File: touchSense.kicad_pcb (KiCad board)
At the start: 2 copper layers, 100 x 100 mm, 19 parts, among them J1 breakout_MainBoard, J2 CAPTOUC_castellated_Module, J3 CAPTOUC_castellated_Module, J4 CAPTOUC_castellated_Module, J5 CAPTOUC_castellated_Module, J6 CAPTOUC_castellated_Module, M101 Mount, M102 Mount, M103 Mount

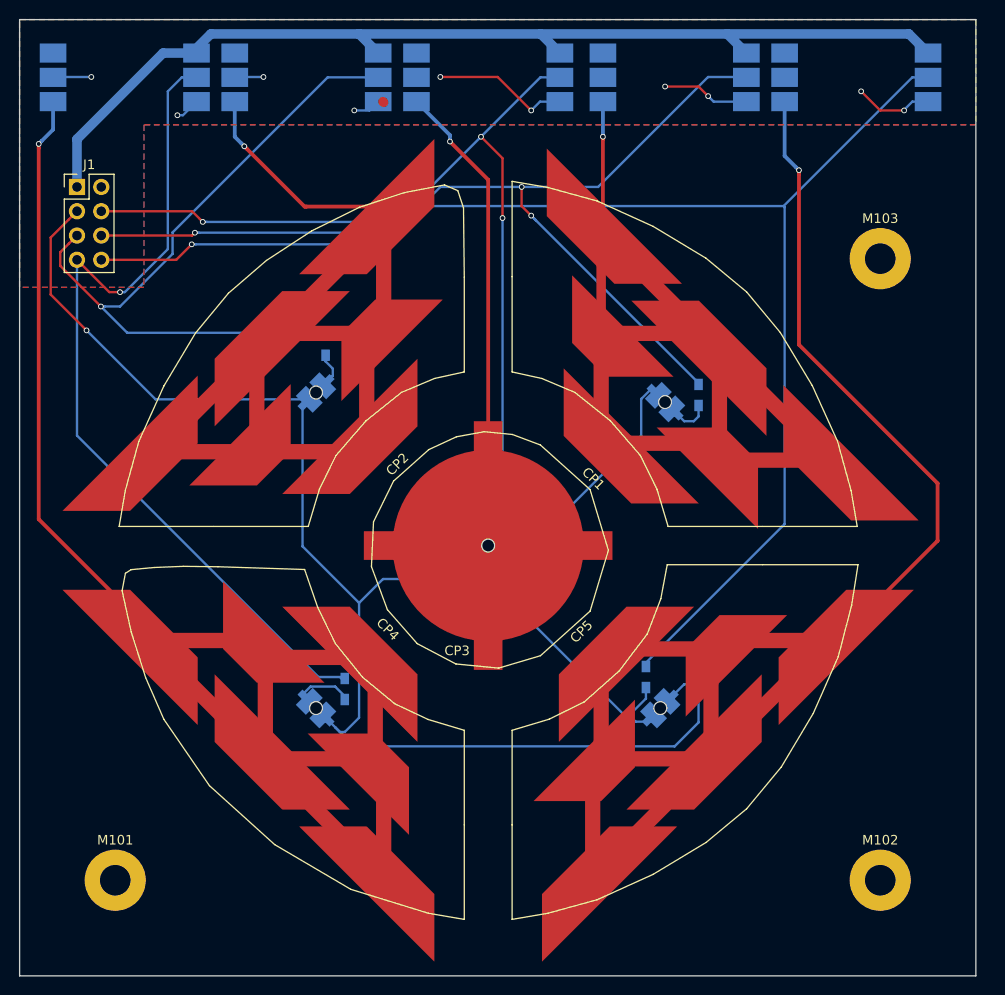
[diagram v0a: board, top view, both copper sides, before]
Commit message: new touch implementation
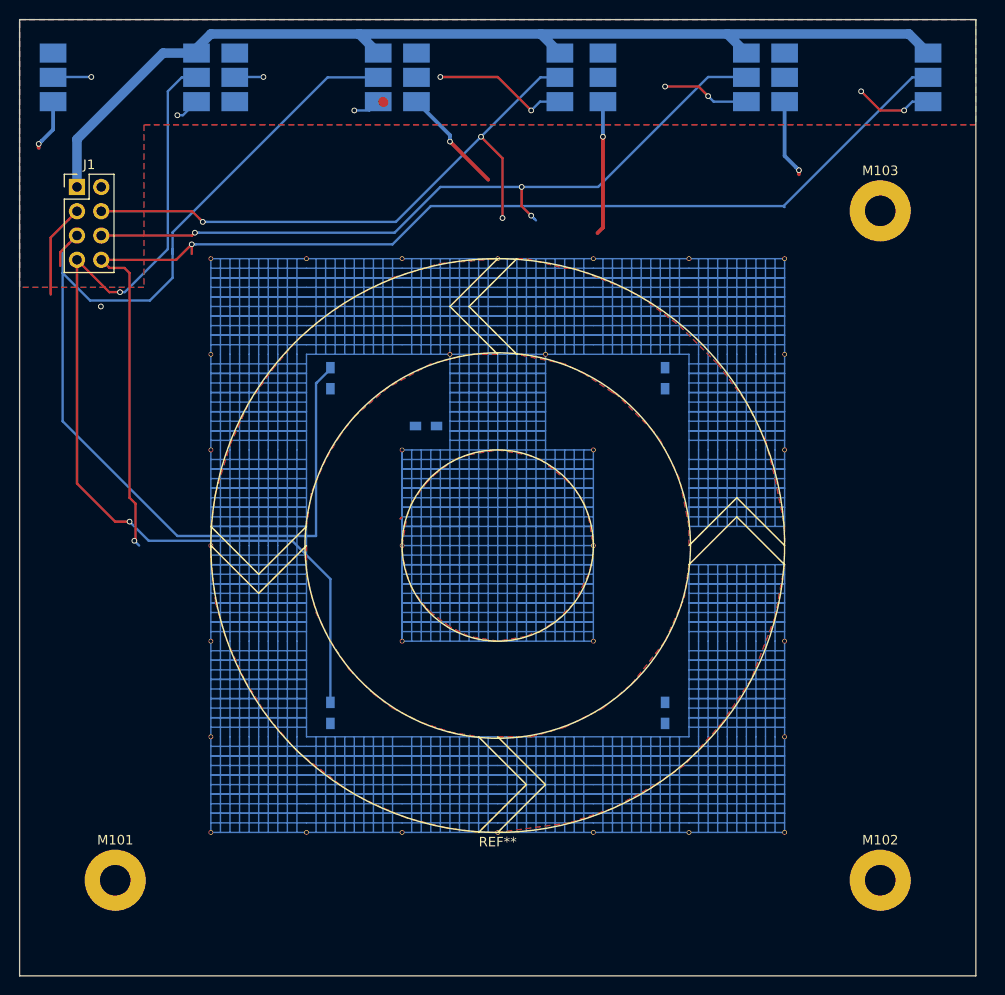
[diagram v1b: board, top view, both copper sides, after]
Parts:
- removed CP1, CP2, CP4, CP5: CAP_PAD_LED, seniorDesign:capacitive_touch_pad_r2
- removed CP3: CAP_PAD_LED, seniorDesign:capacitive_touch_pad_r4
- added J101: HATCHED_FILL, seniorDesign:HATCHED_FILL_60mm_signalRouting, B.Cu at (150.0, 105.0)
- added REF**: CAP_PAD_5POS, seniorDesign:CAP_PAD_5POS_Outline, F.Cu at (150.0, 105.0)
- moved R3 9.42 mm to (142.5, 92.5), turned to 180 degrees
- moved M103 5.00 mm to (190.0, 70.0)
- moved R5 4.25 mm to (167.5, 122.5)
- moved R1 3.91 mm to (167.5, 87.5)
- moved R2 3.54 mm to (132.5, 87.5)
- moved R4 2.92 mm to (132.5, 122.5)
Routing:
- net GND: track 243.5 -> 54.3 mm, vias 11 -> 10
- net /CAP_5: track 174.9 -> 8.22 mm
- net /CAP_4: track 168.4 -> 5.47 mm
- net /CAP_2: track 129.1 -> 0.00 mm, vias 1 -> 0
- net /CAP_1: track 120.1 -> 14.0 mm
- net /CAP_3: track 60.1 -> 11.9 mm
- net /OUT_2: track 75.2 -> 121.0 mm, vias 1 -> 0
- net /OUT_3: track 95.8 -> 64.2 mm
- net /OUT_1: track 103.6 -> 78.8 mm
- net /OUT_5: track 149.8 -> 128.9 mm, vias 1 -> 2
- net /OUT_4: track 89.9 -> 99.8 mm, vias 1 -> 2
- net Net-(CP5-Pad2): track 6.88 -> 0.00 mm
- net Net-(CP4-Pad2): track 6.17 -> 0.00 mm
- net Net-(CP3-Pad2): track 5.85 -> 0.00 mm
- net Net-(CP1-Pad2): track 5.04 -> 0.00 mm
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- added copper zone on F.Cu, net /CAP_1
- added copper zone on F.Cu, net /CAP_2
- added copper zone on F.Cu, net /CAP_4
- added copper zone on F.Cu, net /CAP_5

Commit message: organize project folder, small pcb maitenance, generated gerbers
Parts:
- removed REF**: CAP_PAD_5POS, seniorDesign:CAP_PAD_5POS_Outline
- added D101: LED, seniorDesign:LED_VLRK31Q1R2_REV_GUL, B.Cu at (160.0, 101.0)
- added D102: LED, seniorDesign:LED_VLRK31Q1R2_REV_GUL, B.Cu at (140.0, 101.0)
- added D103: LED, seniorDesign:LED_VLRK31Q1R2_REV_GUL, B.Cu at (150.0, 113.0)
- added D104: LED, seniorDesign:LED_VLRK31Q1R2_REV_GUL, B.Cu at (140.0, 125.0)
- added D105: LED, seniorDesign:LED_VLRK31Q1R2_REV_GUL, B.Cu at (160.0, 125.0)
- added M101: Mount, Mounting_Holes:MountingHole_3.2mm_M3_Pad, F.Cu at (107.0, 83.0)
- J1: moved to B.Cu
- moved J1 45.1 mm to (151.0, 65.0), turned to 180 degrees
- moved R3 20.5 mm to (143.0, 113.0)
- moved R1 19.8 mm to (153.0, 101.0), turned to 180 degrees
- moved R2 18.1 mm to (137.2, 105.0), turned to 270 degrees
- moved M103 13.3 mm to (193.0, 83.0)
- moved J101 8.00 mm to (150.0, 113.0), turned to 0 degrees
- moved R4 4.98 mm to (137.2, 121.0)
- moved R5 4.98 mm to (162.8, 121.0)
- moved M101 4.24 mm to (107.0, 143.0)
- moved M102 4.24 mm to (193.0, 143.0)
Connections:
- J1 pad 4: /OUT_3 -> /OUT_4
- J1 pad 6: /OUT_1 -> /OUT_3
- J1 pad 7: /OUT_4 -> /OUT_1
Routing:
- net GND: track 54.3 -> 166.0 mm, vias 10 -> 2
- net /CAP_2: track 0.00 -> 83.0 mm, vias 0 -> 1
- net /CAP_4: track 5.47 -> 70.0 mm
- net /CAP_5: track 8.22 -> 71.3 mm
- net /OUT_1: track 78.8 -> 140.4 mm, vias 3 -> 1
- net /OUT_5: track 128.9 -> 185.8 mm, vias 2 -> 1
- net /OUT_3: track 64.2 -> 118.1 mm
- net /OUT_4: track 99.8 -> 140.4 mm, vias 2 -> 1
- net /CAP_3: track 11.9 -> 28.9 mm
- net /CAP_1: track 14.0 -> 29.2 mm
- net /OUT_2: track 121.0 -> 132.2 mm, vias 0 -> 2
- net /VCC: track 108.2 -> 98.2 mm
- net Net-(D103-Pad2): track 0.00 -> 3.15 mm
- net Net-(D101-Pad2): track 0.00 -> 3.15 mm
- net Net-(D105-Pad2): track 0.00 -> 2.90 mm
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- removed copper zone on F.Cu, net GND
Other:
- board text added: "VCC GND GND OUT5 OUT1 OUT4 OUT2 OUT3"
- board text removed: "VCC GND GND OUT3 OUT1 OUT4 OUT2 OUT5"

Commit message: after mock cdr
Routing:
- net /CAP_2: track 83.0 -> 85.6 mm
- net /OUT_5: track 185.8 -> 184.7 mm
- net /OUT_1: track 140.4 -> 139.8 mm
